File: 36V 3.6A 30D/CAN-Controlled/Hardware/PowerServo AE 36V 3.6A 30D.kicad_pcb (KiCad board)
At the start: 4 copper layers, 30 x 35.7 mm, 31 parts, among them IC1 DRV8251DDAR, J1 Control_In, J2 MOT_A, J3 Prog_IN, J4 Power_In, J6 Control_In, J7 MOT_B, U1 LMZM23601V5, U2 TLV76733DRVx, U4 MA730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

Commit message: idem
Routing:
- net GND: track 19.9 -> 21.8 mm, vias 143 -> 156
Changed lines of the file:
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@@
+	)
+	(segment
+		(start 87.65 73.15)
+		(end 87.25 72.75)
+		(width 0.508)
+		(layer "F.Cu")
+		(net 1)
 	)
 	(segment
@@
 	(segment
 		(start 87.65 73.15)
-		(end 87.25 72.75)
+		(end 87.25 73.25)
 		(width 0.508)
 		(layer "F.Cu")
@@
 	)
 	(segment
+		(start 87.25 73.25)
+		(end 86.75 72.75)
+		(width 0.508)
+		(layer "F.Cu")
+		(net 1)
+	)
+	(segment
 		(start 101.25 68.25)
 		(end 101.613288 68.25)
@@
 	)
 	(segment
+		(start 86.75 72.75)
+		(end 87.25 72.25)
+		(width 0.508)
+		(layer "F.Cu")
+		(net 1)
+	)
+	(segment
 		(start 90.85 73.15)
 		(end 91.75 72.25)
@@
 	)
 	(via
+		(at 86.75 72.75)
+		(size 0.6)
+		(drill 0.3)
+		(layers "F.Cu" "B.Cu")
+		(net 1)
+	)
+	(via
 		(at 93.15 86.05)
 		(size 0.6)
@@
 	)
 	(via
+		(at 85.25 73.25)
+		(size 0.6)
+		(drill 0.3)
+		(layers "F.Cu" "B.Cu")
+		(net 1)
+	)
+	(via
 		(at 81.5 71)
 		(size 0.6)
@@
 	)
 	(via
+		(at 84.75 71.75)
+		(size 0.6)
+		(drill 0.3)
+		(layers "F.Cu" "B.Cu")
+		(net 1)
+	)
+	(via
 		(at 87.55 56.45)
 		(size 0.6)
@@
 	)
 	(via
+		(at 86.75 73.75)
+		(size 0.6)
+		(drill 0.3)
+		(layers "F.Cu" "B.Cu")
+		(net 1)
+	)
+	(via
 		(at 82.75 66.85)
 		(size 0.6)
@@
 	)
 	(via
+		(at 84.75 72.75)
+		(size 0.6)
+		(drill 0.3)
+		(layers "F.Cu" "B.Cu")
+		(net 1)
+	)
+	(via
 		(at 80.35 69.25)
 		(size 0.6)
@@
 	)
 	(via
+		(at 85.75 73.75)
+		(size 0.6)
+		(drill 0.3)
+		(layers "F.Cu" "B.Cu")
+		(net 1)
+	)
+	(via
 		(at 81.5 74.5)
 		(size 0.6)
@@
 	)
 	(via
+		(at 85.75 72.75)
+		(size 0.6)
+		(drill 0.3)
+		(layers "F.Cu" "B.Cu")
+		(net 1)
+	)
+	(via
 		(at 88.25 59.2)
 		(size 0.6)
@@
 	)
 	(via
+		(at 86.25 72.25)
+		(size 0.6)
+		(drill 0.3)
+		(layers "F.Cu" "B.Cu")
+		(net 1)
+	)
+	(via
 		(at 97.15 61.25)
 		(size 0.6)
@@
 	)
 	(via
+		(at 85.25 72.25)
+		(size 0.6)
+		(drill 0.3)
+		(layers "F.Cu" "B.Cu")
+		(net 1)
+	)
+	(via
 		(at 82.75 66.05)
 		(size 0.6)
@@
 	)
 	(via
+		(at 86.25 73.25)
+		(size 0.6)
+		(drill 0.3)
+		(layers "F.Cu" "B.Cu")
+		(net 1)
+	)
+	(via
 		(at 102.75 82.85)
 		(size 0.6)
@@
 	)
 	(via
+		(at 87.25 72.25)
+		(size 0.6)
+		(drill 0.3)
+		(layers "F.Cu" "B.Cu")
+		(net 1)
+	)
+	(via
 		(at 101.681644 68.181644)
 		(size 0.6)
@@
 	)
 	(via
+		(at 87.25 73.25)
+		(size 0.6)
+		(drill 0.3)
+		(layers "F.Cu" "B.Cu")
+		(net 1)
+	)
+	(via
 		(at 101.95 62.05)
 		(size 0.6)
@@
 		(net 1)
 	)
+	(via
+		(at 84.75 73.75)
+		(size 0.6)
+		(drill 0.3)
+		(layers "F.Cu" "B.Cu")
+		(net 1)
+	)

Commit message: Dev Version for Tests
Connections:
- IC1 pad 7: Net-(IC1-ISEN) -> ISEN
- R1 pad 1: Net-(IC1-ISEN) -> ISEN
- U7 pad 10: unconnected-(U7-PA3-Pad10) -> ISEN
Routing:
- net ISEN: track 0.00 -> 11.2 mm, vias 0 -> 2
- net Net-(IC1-ISEN): track 2.69 -> 0.00 mm, vias 1 -> 0

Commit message: Flow
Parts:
- added J5: Power_In, Connector_AMASS:AMASS_XT30UPB-M_1x02_P5.0mm_Vertical, F.Cu at (111.0, 75.8)
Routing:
- net GND: track 21.8 -> 24.1 mm, vias 156 -> 151
- added copper zone on F.Cu, net +12V
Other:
- board size 30 x 35.7 mm -> 35.7 x 35.5 mm

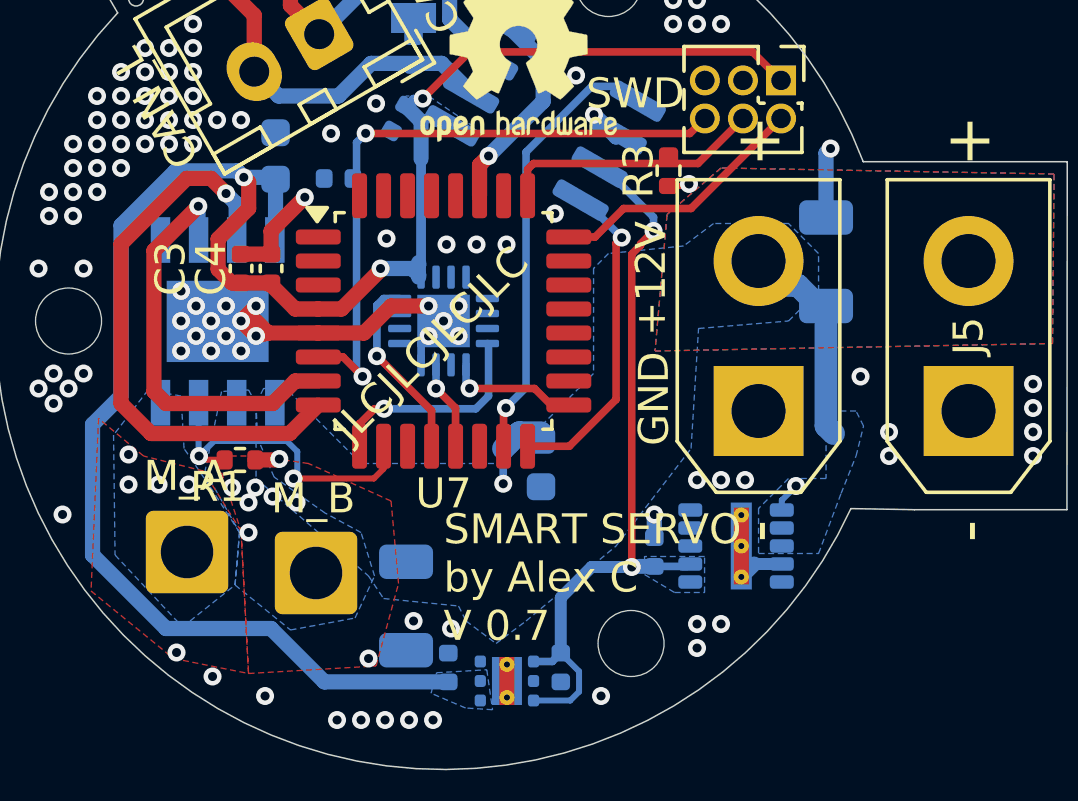
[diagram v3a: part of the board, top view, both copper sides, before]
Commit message: Flowchart update. PCB Update to include 2nd XT30
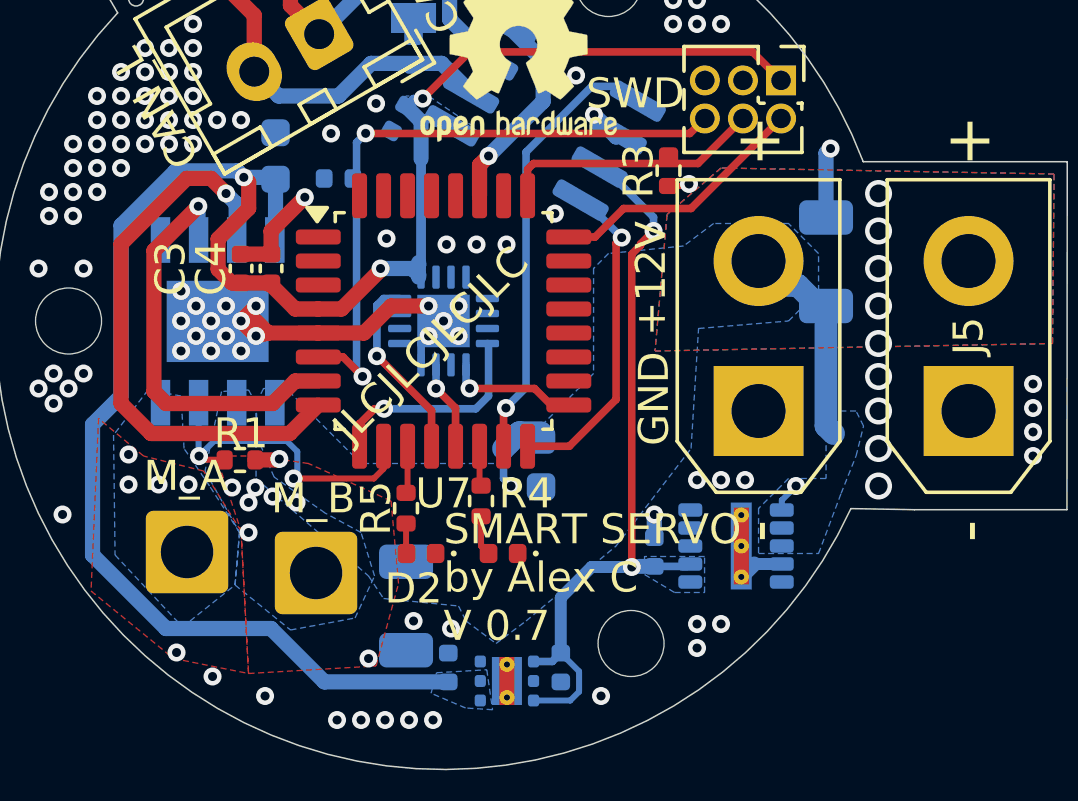
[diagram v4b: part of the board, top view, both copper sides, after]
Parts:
- added D1: LED, LED_SMD:LED_0402_1005Metric, F.Cu at (95.5, 80.5)
- added D2: LED, LED_SMD:LED_0402_1005Metric, F.Cu at (92.8, 80.5)
- added R4: 430, Resistor_SMD:R_0402_1005Metric, F.Cu at (94.8, 78.8)
- added R5: 430, Resistor_SMD:R_0402_1005Metric, F.Cu at (92.3, 79.0)
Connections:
- U7 pad 11: unconnected-(U7-PA4-Pad11) -> Net-(U7-PA4)
- U7 pad 14: unconnected-(U7-PA7-Pad14) -> Net-(U7-PA7)
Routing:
- net Net-(U7-PA4): track 0.00 -> 1.58 mm
- net Net-(D1-Pad2): track 0.00 -> 1.34 mm
- net Net-(U7-PA7): track 0.00 -> 1.34 mm
- net Net-(D2-Pad2): track 0.00 -> 1.01 mm
- net GND: track 24.1 -> 24.3 mm, vias 151 -> 152
- net +12V: vias 0 -> 5

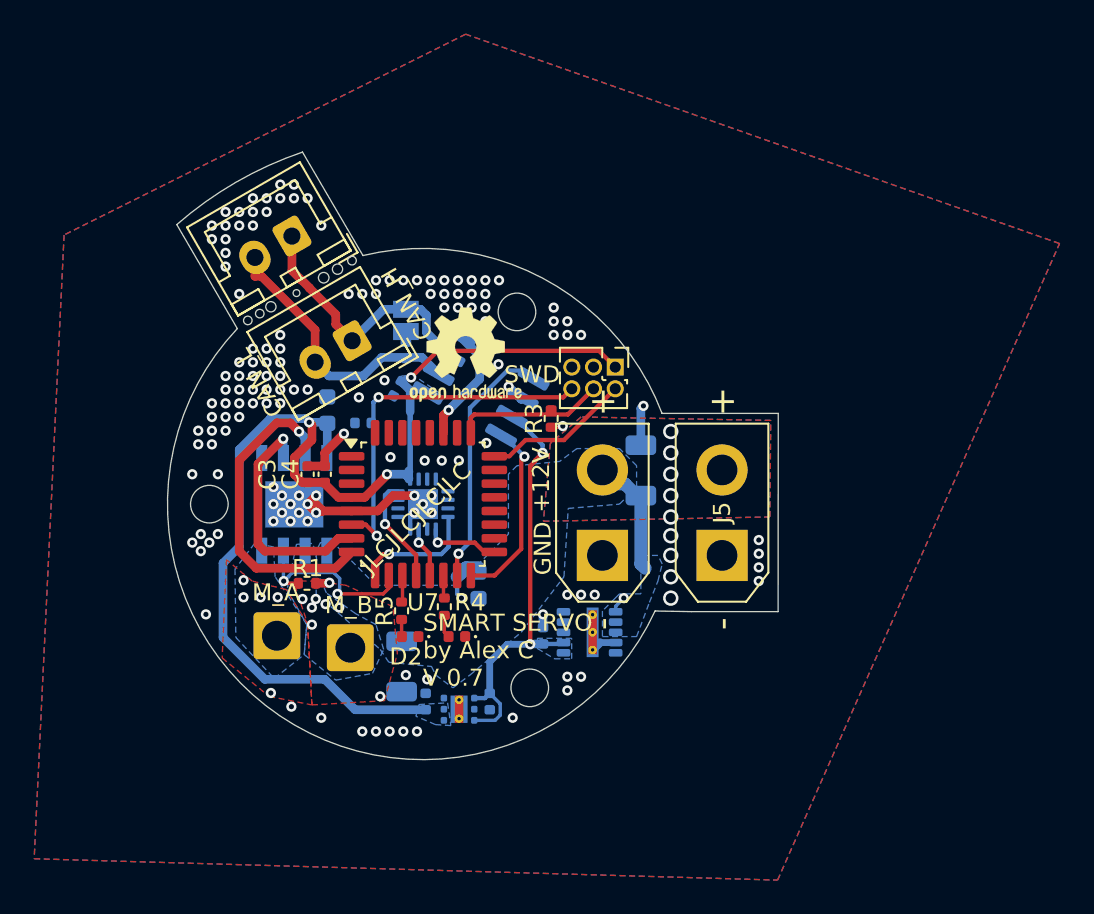
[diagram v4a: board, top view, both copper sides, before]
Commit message: Solved DRC
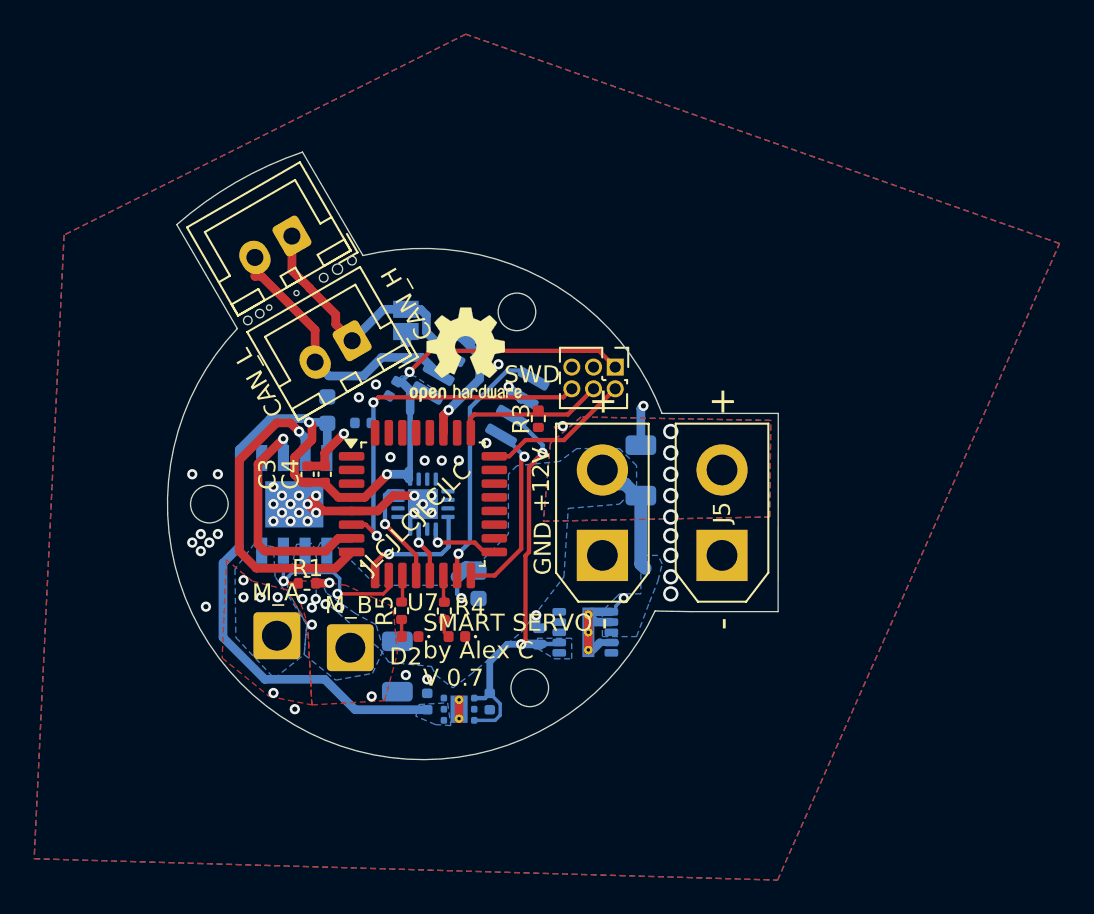
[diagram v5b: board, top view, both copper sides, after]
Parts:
- moved R3 0.75 mm to (100.2, 67.8)
- moved C1 0.28 mm to (100.2, 80.5)
- moved C7 0.25 mm to (92.0, 82.2)
- moved C9 0.25 mm to (91.8, 66.0)
- moved R4 0.25 mm to (94.8, 79.0)
- moved U1 0.25 mm to (103.0, 80.2)
- moved C6 0.09 mm to (93.8, 84.3)
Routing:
- net GND: track 24.3 -> 27.3 mm, vias 152 -> 51
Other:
- outline, holes or cut-outs redrawn

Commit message: Exports
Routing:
- net GND: vias 51 -> 152
